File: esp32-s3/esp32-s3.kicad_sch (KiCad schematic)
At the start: 0 parts

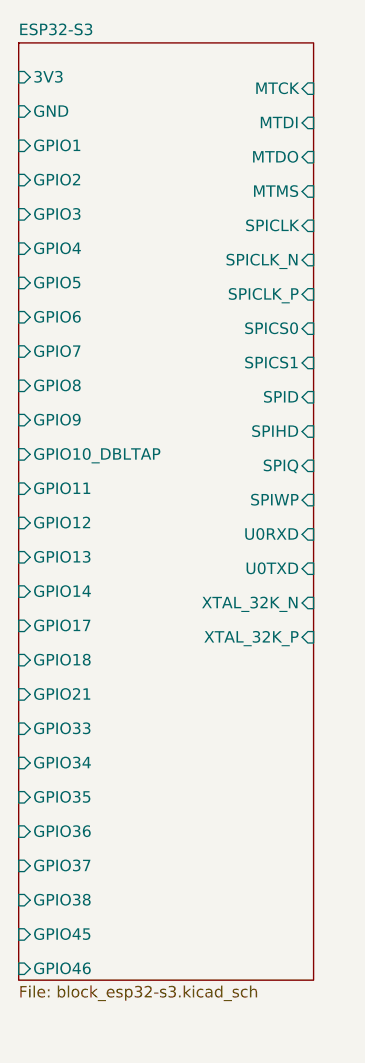
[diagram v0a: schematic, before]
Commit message: [Rushil] added ldo
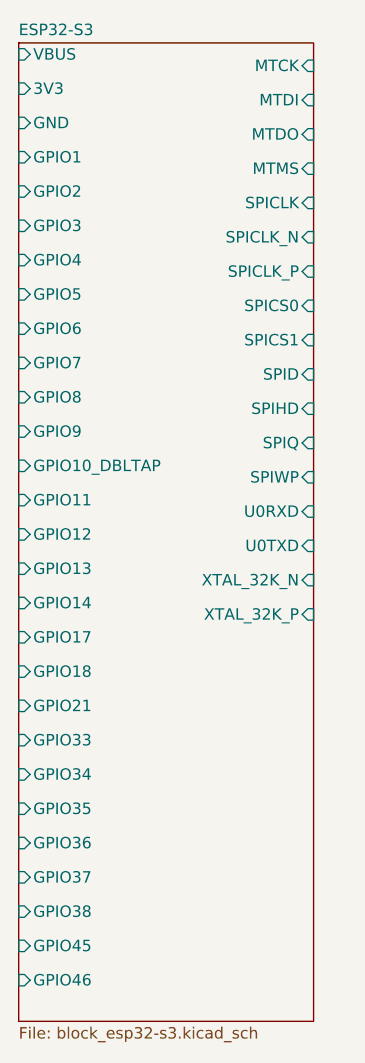
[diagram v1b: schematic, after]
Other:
- sheet ESP32-S3 ports: added VBUS; removed none
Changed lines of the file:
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@@
 	(sheet
 		(at 101.854 45.72)
-		(size 32.766 104.14)
+		(size 32.766 108.712)
 		(exclude_from_sim no)
 		(in_bom yes)
@@
 		)
 		(property "Sheetfile" "block_esp32-s3.kicad_sch"
-			(at 101.854 150.4446 0)
+			(at 101.854 155.0166 0)
 			(effects
 				(font
@@
 		)
 		(pin "3V3" input
-			(at 101.854 49.53 180)
+			(at 101.854 50.8 180)
 			(effects
 				(font
@@
 		)
 		(pin "GND" input
-			(at 101.854 53.34 180)
+			(at 101.854 54.61 180)
 			(effects
 				(font
@@
 		)
 		(pin "GPIO1" input
-			(at 101.854 57.15 180)
+			(at 101.854 58.42 180)
 			(effects
 				(font
@@
 		)
 		(pin "GPIO2" input
-			(at 101.854 60.96 180)
+			(at 101.854 62.23 180)
 			(effects
 				(font
@@
 		)
 		(pin "GPIO3" input
-			(at 101.854 64.77 180)
+			(at 101.854 66.04 180)
 			(effects
 				(font
@@
 		)
 		(pin "GPIO4" input
-			(at 101.854 68.58 180)
+			(at 101.854 69.85 180)
 			(effects
 				(font
@@
 		)
 		(pin "GPIO5" input
-			(at 101.854 72.39 180)
+			(at 101.854 73.66 180)
 			(effects
 				(font
@@
 		)
 		(pin "GPIO6" input
-			(at 101.854 76.2 180)
+			(at 101.854 77.47 180)
 			(effects
 				(font
@@
 		)
 		(pin "GPIO7" input
-			(at 101.854 80.01 180)
+			(at 101.854 81.28 180)
 			(effects
 				(font
@@
 		)
 		(pin "GPIO8" input
-			(at 101.854 83.82 180)
+			(at 101.854 85.09 180)
 			(effects
 				(font
@@
 		)
 		(pin "GPIO9" input
-			(at 101.854 87.63 180)
+			(at 101.854 88.9 180)
 			(effects
 				(font
@@
 		)
 		(pin "GPIO10_DBLTAP" input
-			(at 101.854 91.44 180)
+			(at 101.854 92.71 180)
 			(effects
 				(font
@@
 		)
 		(pin "GPIO11" input
-			(at 101.854 95.25 180)
+			(at 101.854 96.52 180)
 			(effects
 				(font
@@
 		)
 		(pin "GPIO12" input
-			(at 101.854 99.06 180)
+			(at 101.854 100.33 180)
 			(effects
 				(font
@@
 		)
 		(pin "GPIO13" input
-			(at 101.854 102.87 180)
+			(at 101.854 104.14 180)
 			(effects
 				(font
@@
 		)
 		(pin "GPIO14" input
-			(at 101.854 106.68 180)
+			(at 101.854 107.95 180)
 			(effects
 				(font
@@
 		)
 		(pin "GPIO17" input
-			(at 101.854 110.49 180)
+			(at 101.854 111.76 180)
 			(effects
 				(font
@@
 		)
 		(pin "GPIO18" input
-			(at 101.854 114.3 180)
+			(at 101.854 115.57 180)
 			(effects
 				(font
@@
 		)
 		(pin "GPIO21" input
-			(at 101.854 118.11 180)
+			(at 101.854 119.38 180)
 			(effects
 				(font
@@
 		)
 		(pin "GPIO33" input
-			(at 101.854 121.92 180)
+			(at 101.854 123.19 180)
 			(effects
 				(font
@@
 		)
 		(pin "GPIO34" input
-			(at 101.854 125.73 180)
+			(at 101.854 127 180)
 			(effects
 				(font
@@
 		)
 		(pin "GPIO35" input
-			(at 101.854 129.54 180)
+			(at 101.854 130.81 180)
 			(effects
 				(font
@@
 		)
 		(pin "GPIO36" input
-			(at 101.854 133.35 180)
+			(at 101.854 134.62 180)
 			(effects
 				(font
@@
 		)
 		(pin "GPIO37" input
-			(at 101.854 137.16 180)
+			(at 101.854 138.43 180)
 			(effects
 				(font
@@
 		)
 		(pin "GPIO38" input
-			(at 101.854 140.97 180)
+			(at 101.854 142.24 180)
 			(effects
 				(font
@@
 		)
 		(pin "GPIO45" input
-			(at 101.854 144.78 180)
+			(at 101.854 146.05 180)
 			(effects
 				(font
@@
 		)
 		(pin "GPIO46" input
-			(at 101.854 148.59 180)
+			(at 101.854 149.86 180)
 			(effects
 				(font
@@
 		)
 		(pin "MTCK" input
-			(at 134.62 50.8 0)
+			(at 134.62 48.26 0)
 			(effects
 				(font
@@
 		)
 		(pin "MTDI" input
-			(at 134.62 54.61 0)
+			(at 134.62 52.07 0)
 			(effects
 				(font
@@
 		)
 		(pin "MTDO" input
-			(at 134.62 58.42 0)
+			(at 134.62 55.88 0)
 			(effects
 				(font
@@
 		)
 		(pin "MTMS" input
-			(at 134.62 62.23 0)
+			(at 134.62 59.69 0)
 			(effects
 				(font
@@
 		)
 		(pin "SPICLK" input
-			(at 134.62 66.04 0)
+			(at 134.62 63.5 0)
 			(effects
 				(font
@@
 		)
 		(pin "SPICLK_N" input
-			(at 134.62 69.85 0)
+			(at 134.62 67.31 0)
 			(effects
 				(font
@@
 		)
 		(pin "SPICLK_P" input
-			(at 134.62 73.66 0)
+			(at 134.62 71.12 0)
 			(effects
 				(font
@@
 		)
 		(pin "SPICS0" input
-			(at 134.62 77.47 0)
+			(at 134.62 74.93 0)
 			(effects
 				(font
@@
 		)
 		(pin "SPICS1" input
-			(at 134.62 81.28 0)
+			(at 134.62 78.74 0)
 			(effects
 				(font
@@
 		)
 		(pin "SPID" input
-			(at 134.62 85.09 0)
+			(at 134.62 82.55 0)
 			(effects
 				(font
@@
 		)
 		(pin "SPIHD" input
-			(at 134.62 88.9 0)
+			(at 134.62 86.36 0)
 			(effects
 				(font
@@
 		)
 		(pin "SPIQ" input
-			(at 134.62 92.71 0)
+			(at 134.62 90.17 0)
 			(effects
 				(font
@@
 		)
 		(pin "SPIWP" input
-			(at 134.62 96.52 0)
+			(at 134.62 93.98 0)
 			(effects
 				(font
@@
 		)
 		(pin "U0RXD" input
-			(at 134.62 100.33 0)
+			(at 134.62 97.79 0)
 			(effects
 				(font
@@
 		)
 		(pin "U0TXD" input
-			(at 134.62 104.14 0)
+			(at 134.62 101.6 0)
 			(effects
 				(font
@@
 		)
 		(pin "XTAL_32K_N" input
-			(at 134.62 107.95 0)
+			(at 134.62 105.41 0)
 			(effects
 				(font
@@
 		)
 		(pin "XTAL_32K_P" input
-			(at 134.62 111.76 0)
-			(effects
-				(font
-					(size 1.27 1.27)
-				)
-				(justify right)
-			)
-		)
+			(at 134.62 109.22 0)
+			(effects
+				(font
+					(size 1.27 1.27)
+				)
+				(justify right)
+			)
+		)
+		(pin "VBUS" input
+			(at 101.854 46.99 180)
+			(effects
+				(font
+					(size 1.27 1.27)
+				)
+				(justify left)
+			)
+		)
